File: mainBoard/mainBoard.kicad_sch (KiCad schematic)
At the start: 8 parts, among them Q1 PNP

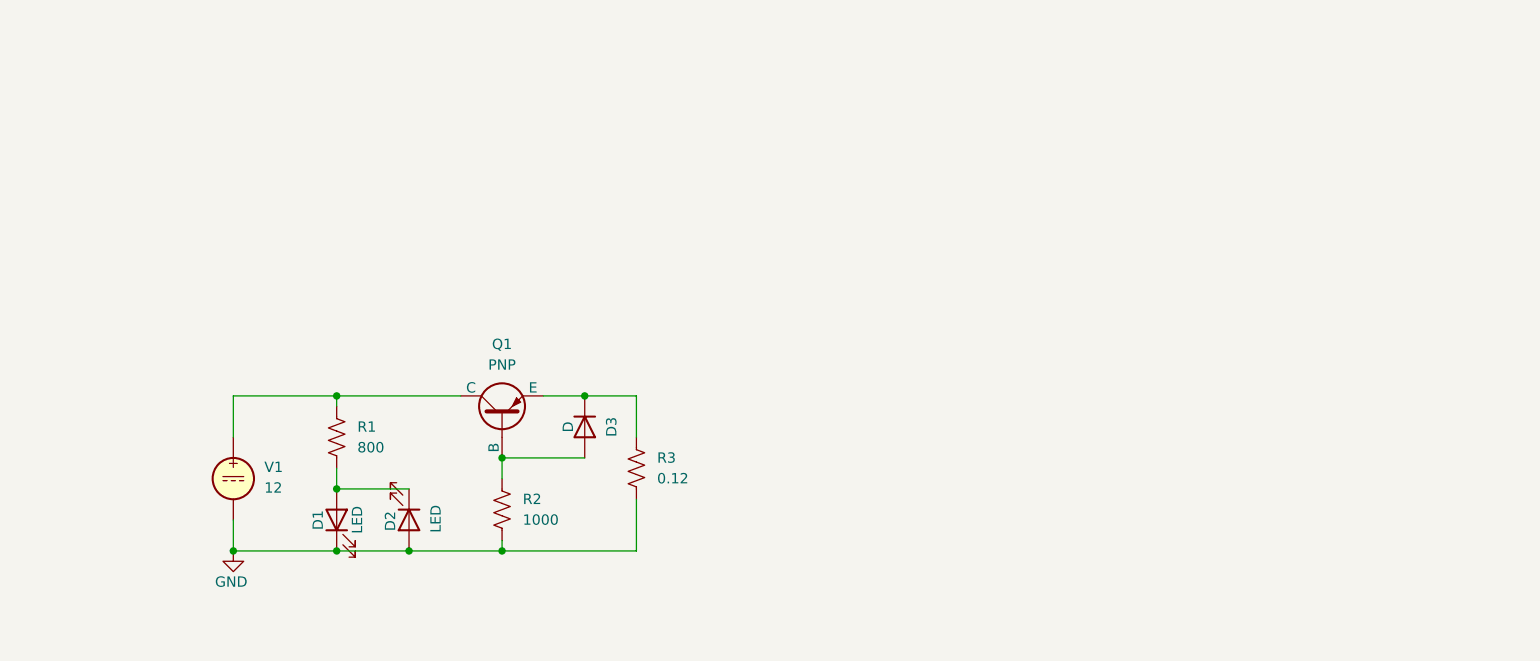
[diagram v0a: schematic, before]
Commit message: Began adding power to the mainboard
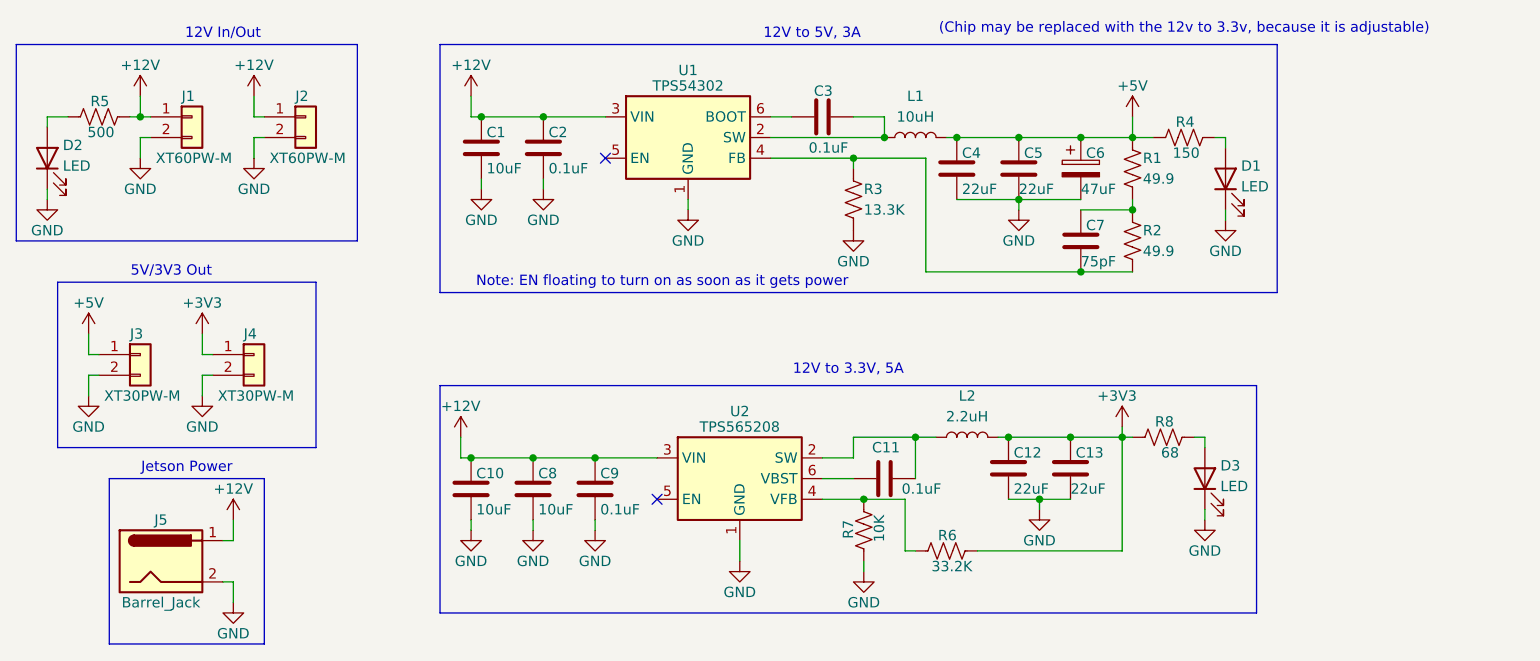
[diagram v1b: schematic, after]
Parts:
- removed D3: D, symbol Simulation_SPICE:D
- removed Q1: PNP, symbol Simulation_SPICE:PNP
- removed V1: 12, symbol Simulation_SPICE:VDC
- added C1, C10, C8: 10uF, Capacitor_SMD:C_0805_2012Metric_Pad1.18x1.45mm_HandSolder, symbol Device:C
- added C11, C2, C3, C9: 0.1uF, Capacitor_SMD:C_0805_2012Metric_Pad1.18x1.45mm_HandSolder, symbol Device:C
- added C12, C13, C4, C5: 22uF, Capacitor_SMD:C_0805_2012Metric_Pad1.18x1.45mm_HandSolder, symbol Device:C
- added C6: 47uF, Capacitor_SMD:CP_Elec_6.3x5.4, symbol Device:C_Polarized
- added C7: 75pF, Capacitor_SMD:C_0805_2012Metric_Pad1.18x1.45mm_HandSolder, symbol Device:C
- added D3: LED, Diode_SMD:D_0805_2012Metric_Pad1.15x1.40mm_HandSolder, symbol Device:LED
- added J1, J2: XT60PW-M, Connector_AMASS:AMASS_XT60PW-M_1x02_P7.20mm_Horizontal, symbol Connector_Generic:Conn_01x02
- added J3, J4: XT30PW-M, Connector_AMASS:AMASS_XT30U-F_1x02_P5.0mm_Vertical, symbol Connector_Generic:Conn_01x02
- added J5: Barrel_Jack, Connector_BarrelJack:BarrelJack_Kycon_KLDX-0202-xC_Horizontal, symbol Connector:Barrel_Jack
- added L1: 10uH, Inductor_SMD:L_Abracon_ASPI-0630LR, symbol Device:L
- added L2: 2.2uH, Inductor_SMD:L_Abracon_ASPI-0630LR, symbol Device:L
- added R4: 150, Resistor_SMD:R_0805_2012Metric_Pad1.20x1.40mm_HandSolder, symbol Device:R_US
- added R5: 500, Resistor_SMD:R_0805_2012Metric_Pad1.20x1.40mm_HandSolder, symbol Device:R_US
- added R6: 33.2K, Resistor_SMD:R_0805_2012Metric_Pad1.20x1.40mm_HandSolder, symbol Device:R_US
- added R7: 10K, Resistor_SMD:R_0805_2012Metric_Pad1.20x1.40mm_HandSolder, symbol Device:R_US
- added R8: 68, Resistor_SMD:R_0805_2012Metric_Pad1.20x1.40mm_HandSolder, symbol Device:R_US
- added U1: TPS54302, Package_TO_SOT_SMD:SOT-23-6, symbol Regulator_Switching:TPS54302
- added U2: TPS565208, Package_TO_SOT_SMD:SOT-23-6, symbol Regulator_Switching:TPS565208
- D1, D2: footprint (none) -> Diode_SMD:D_0805_2012Metric_Pad1.15x1.40mm_HandSolder
- R1: value 800 -> 49.9; footprint (none) -> Resistor_SMD:R_0805_2012Metric_Pad1.20x1.40mm_HandSolder
- R2: value 1000 -> 49.9; footprint (none) -> Resistor_SMD:R_0805_2012Metric_Pad1.20x1.40mm_HandSolder
- R3: value 0.12 -> 13.3K; footprint (none) -> Resistor_SMD:R_0805_2012Metric_Pad1.20x1.40mm_HandSolder
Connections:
- net GND: now also D2.1 (K), R3.2, C1.2, C10.2, C12.2, C13.2, C2.2, C4.2, C5.2, C6.2, C8.2, C9.2, D3.1 (K), J1.2 (Pin_2), J2.2 (Pin_2), J3.2 (Pin_2), J4.2 (Pin_2), J5.2, R7.1, U1.1 (GND), U2.1 (GND); no longer D2.2 (A), R2.1, R3.1
- net at R1.2: now also R2.1, C7.1
- net at R2.2: now also R3.1, C7.2, U1.4 (FB)
- new net: C11.2, L2.1, U2.2 (SW)
- new net: R6.1, R7.2, U2.4 (VFB)
- new net: C11.1, U2.6 (VBST)
- new net: D3.2 (A), R8.2
- new net: D1.2 (A), R4.2
- new net: D2.2 (A), R5.1
- new net: C3.1, U1.6 (BOOT)
- new net: C3.2, L1.1, U1.2 (SW)
- new net +12V: C1.1, C10.1, C2.1, C8.1, C9.1, J1.1 (Pin_1), J2.1 (Pin_1), J5.1, R5.2, U1.3 (VIN), U2.3 (VIN)
- new net +3V3: C12.1, C13.1, J4.1 (Pin_1), L2.2, R6.2, R8.1
- new net +5V: C4.1, C5.1, C6.1, J3.1 (Pin_1), L1.2, R1.1, R4.1
- no-connect marks 0 -> 2
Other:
- note added: "(Chip may be replaced with the 12v to 3.3v, because it is adjustable)"
- note added: "12V In/Out"
- note added: "12V to 3.3V, 5A"
- note added: "12V to 5V, 3A"
- note added: "5V/3V3 Out"
- note added: "Jetson Power"
- note added: "Note: EN floating to turn on as soon as it gets power"

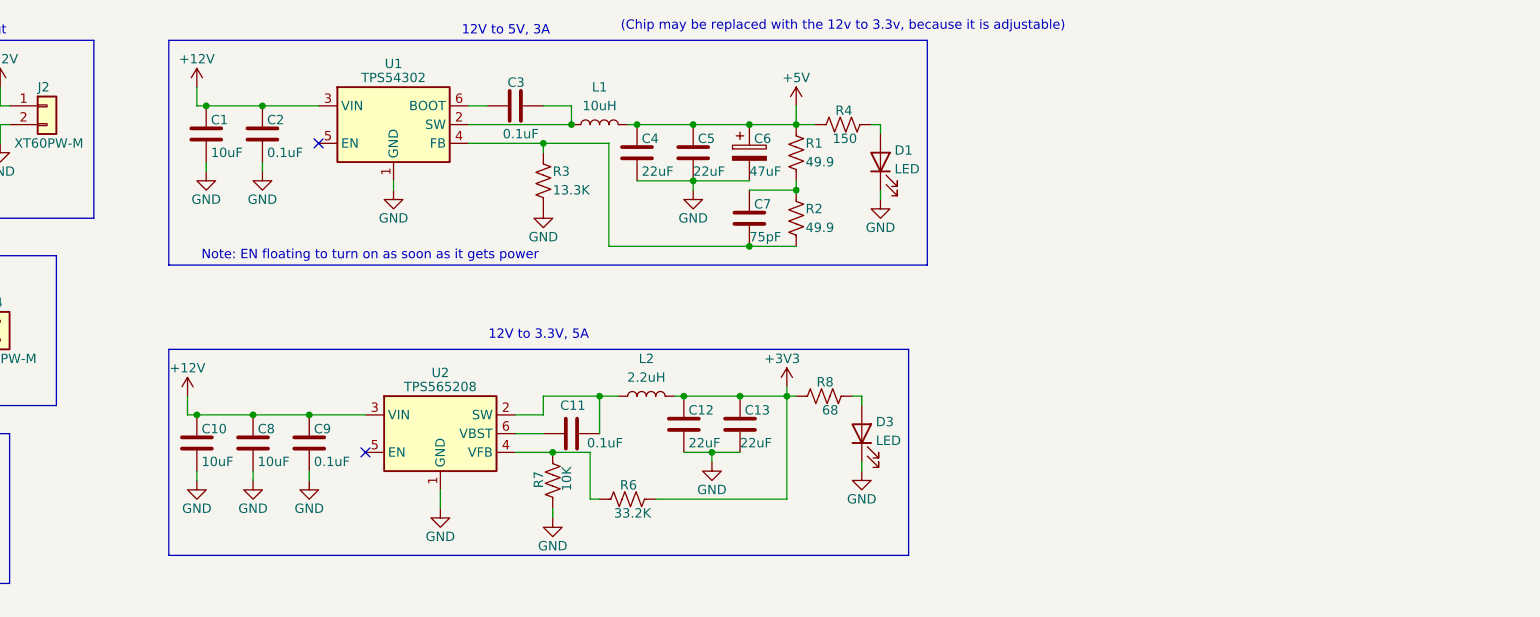
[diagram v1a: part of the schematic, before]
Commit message: Added reverse protection for 5v and 3.3v buck convertors
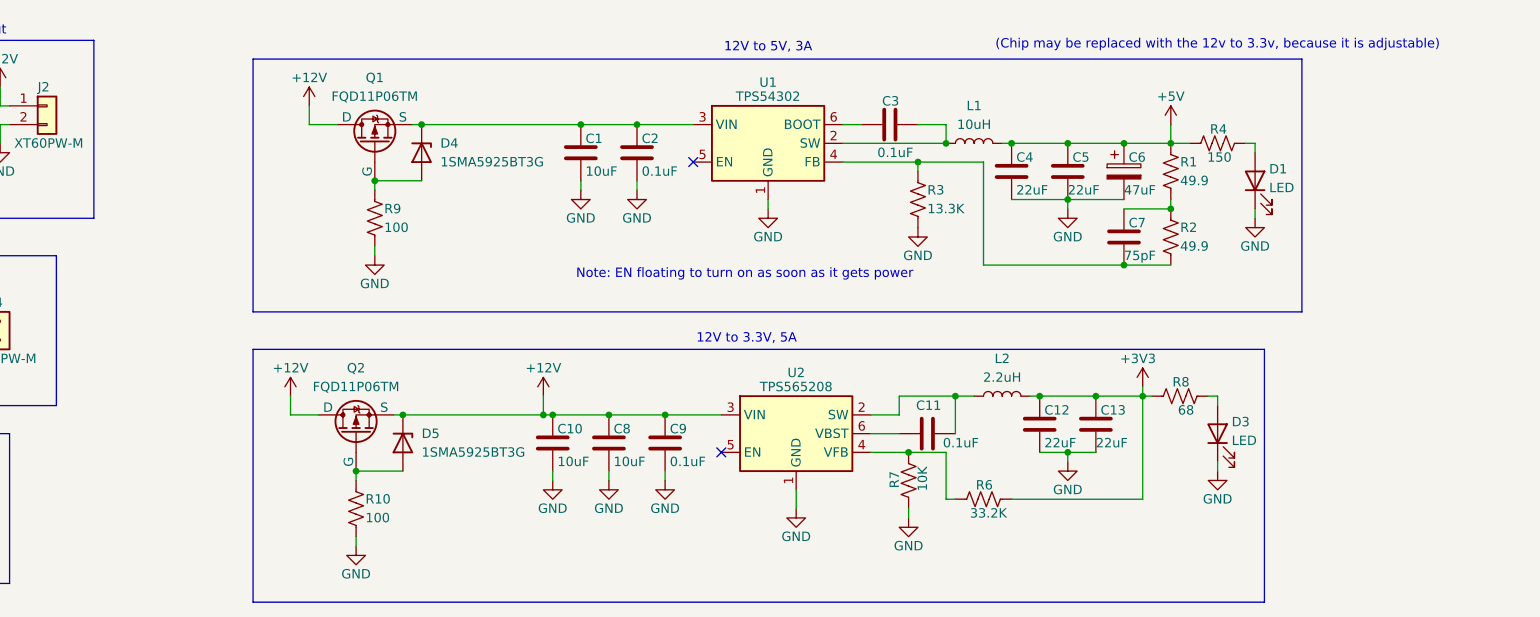
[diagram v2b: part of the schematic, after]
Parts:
- added D4, D5: 1SMA5925BT3G, symbol Device:D_Zener
- added Q1, Q2: FQD11P06TM, Package_TO_SOT_SMD:TO-252-3_TabPin2, symbol Simulation_SPICE:PMOS
- added R10, R9: 100, Resistor_SMD:R_0805_2012Metric_Pad1.20x1.40mm_HandSolder, symbol Device:R_US
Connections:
- net +12V: now also D5.1 (K), Q1.1 (D), Q2.1 (D), Q2.3 (S); no longer C1.1, C2.1, U1.3 (VIN)
- net GND: now also R10.2, R9.2
- new net: D4.2 (A), Q1.2 (G), R9.1
- new net: C1.1, C2.1, D4.1 (K), Q1.3 (S), U1.3 (VIN)
- new net: D5.2 (A), Q2.2 (G), R10.1
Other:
- moved on the sheet: C1, C10, C11, C12, C13, C2, C3, C4, C5, C6, C7, C8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

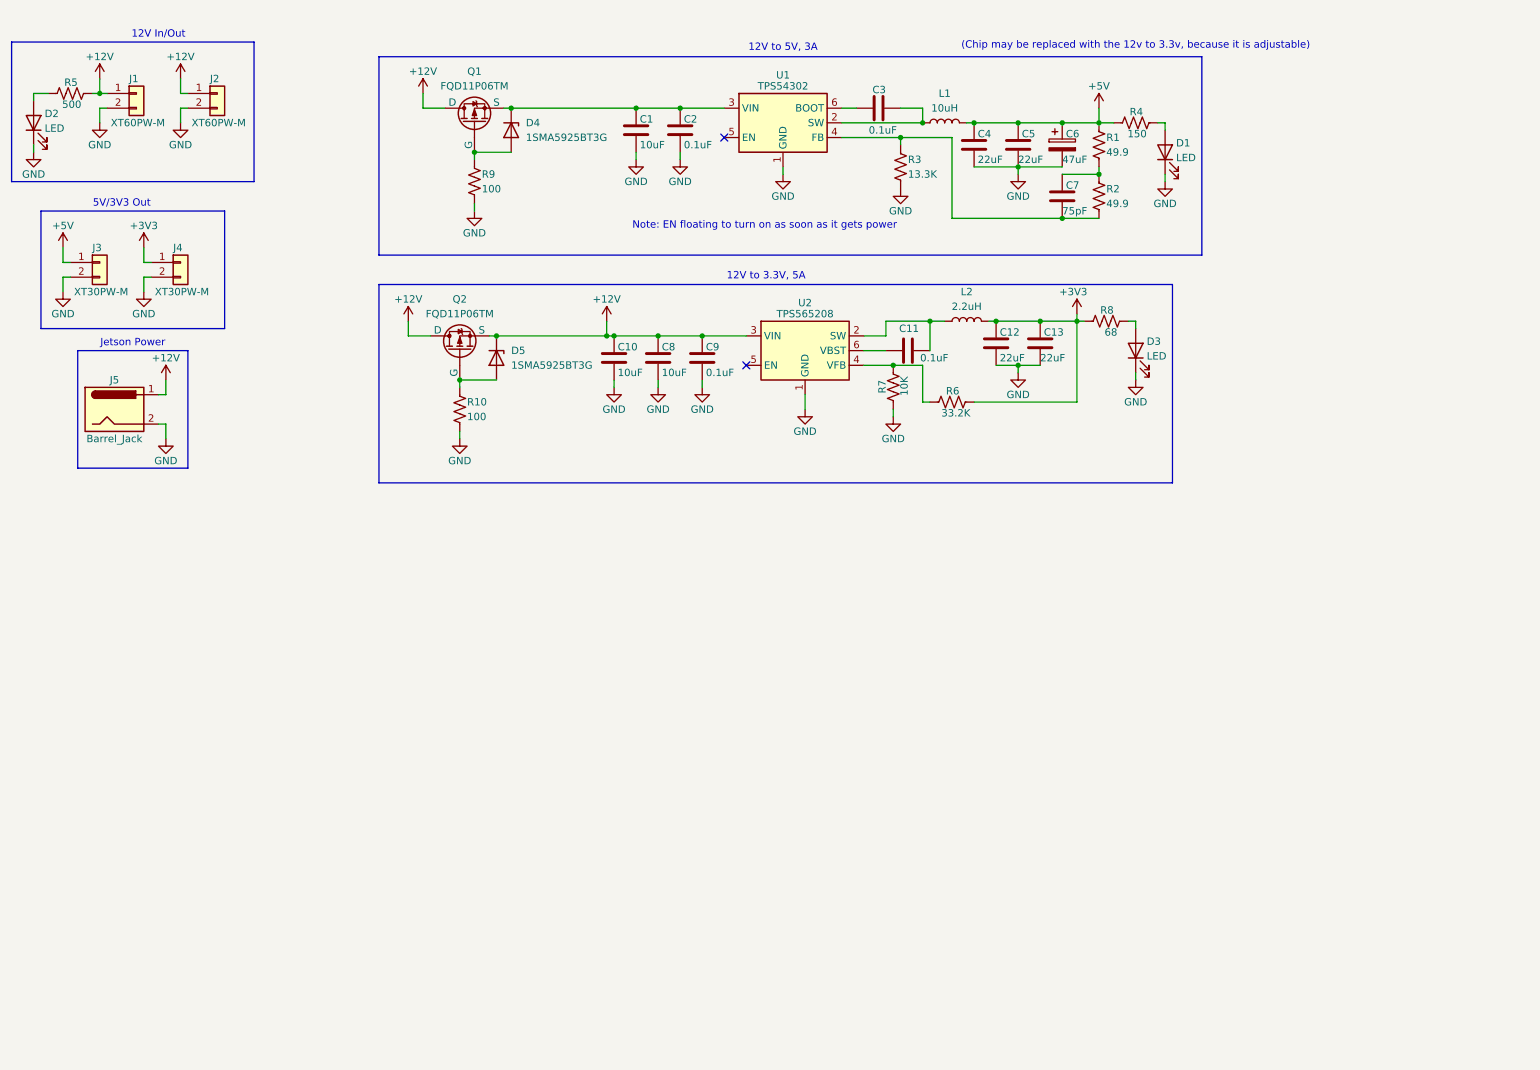
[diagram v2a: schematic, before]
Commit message: Various small things, such as 12v power connectors, jetson header, can stuff, and bypass resistors for reverse protection
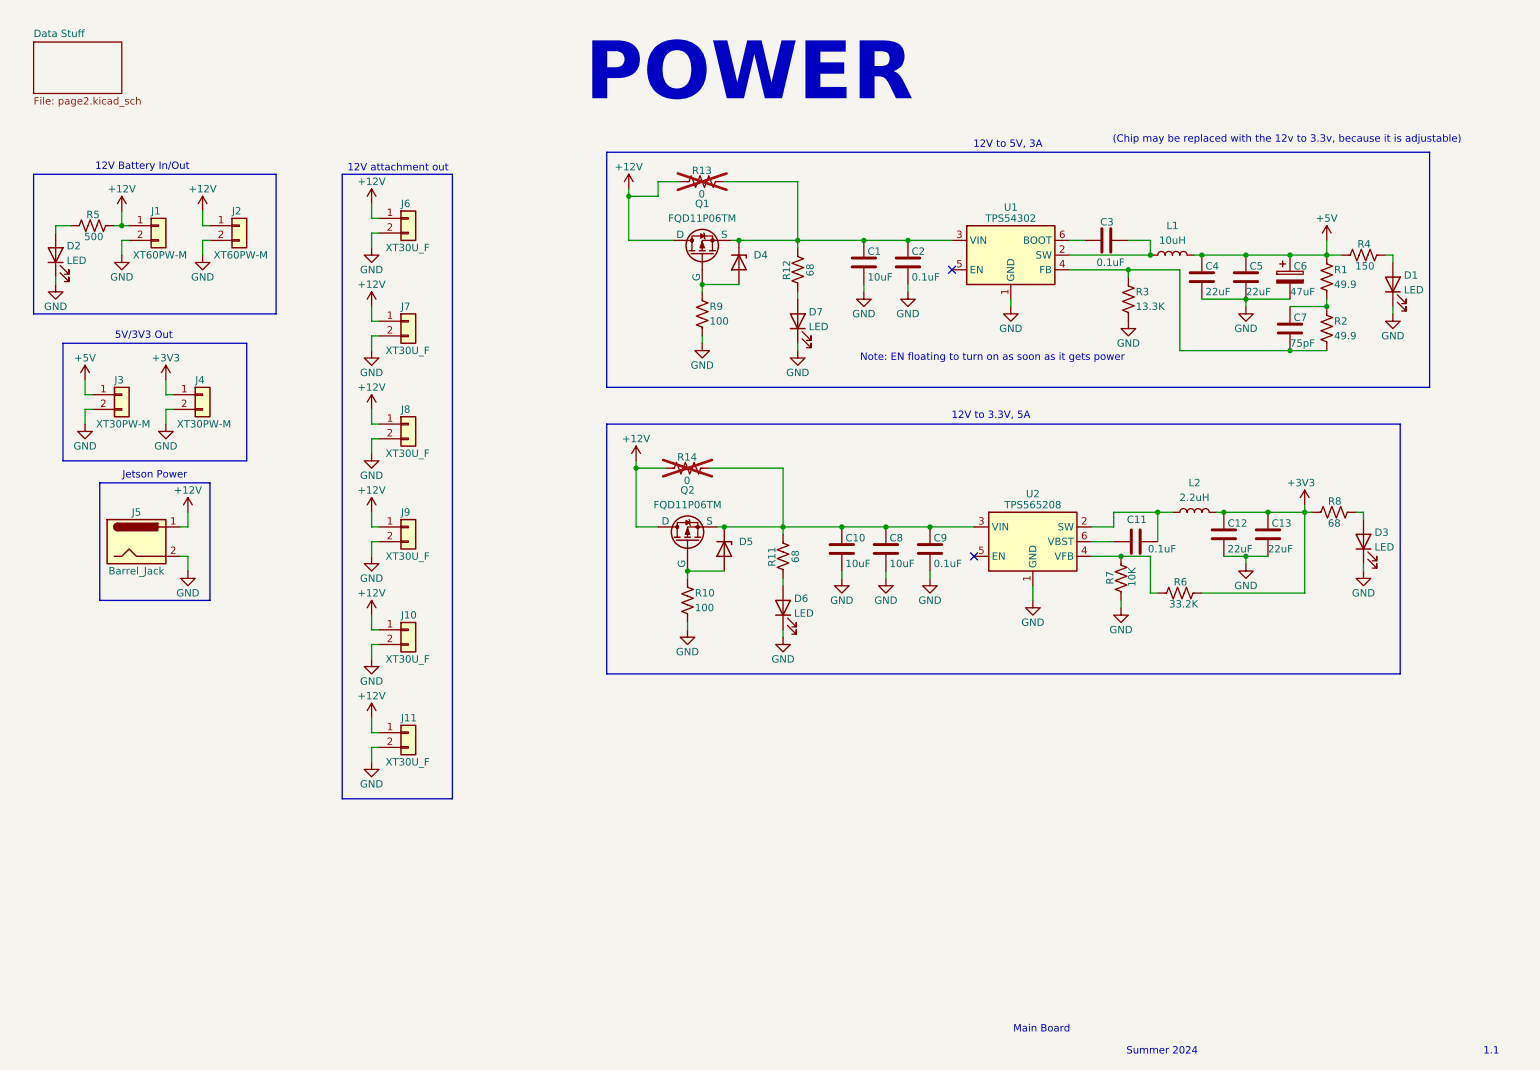
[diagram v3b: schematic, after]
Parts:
- added D6, D7: LED, Diode_SMD:D_0805_2012Metric_Pad1.15x1.40mm_HandSolder, symbol Device:LED
- added J10, J11, J6, J7, J8, J9: XT30U_F, Connector_AMASS:AMASS_XT30U-F_1x02_P5.0mm_Vertical, symbol Connector_Generic:Conn_01x02
- added R11, R12: 68, Resistor_SMD:R_0805_2012Metric_Pad1.20x1.40mm_HandSolder, symbol Device:R_US
- added R13, R14: 0, Resistor_SMD:R_0805_2012Metric_Pad1.20x1.40mm_HandSolder, symbol Device:R_US
- D4, D5: footprint (none) -> Diode_SMD:D_SMA_Handsoldering
- J3, J4: footprint Connector_AMASS:AMASS_XT30U-F_1x02_P5.0mm_Vertical -> Connector_AMASS:AMASS_XT30PW-M_1x02_P2.50mm_Horizontal
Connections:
- net +12V: now also J10.1 (Pin_1), J11.1 (Pin_1), J6.1 (Pin_1), J7.1 (Pin_1), J8.1 (Pin_1), J9.1 (Pin_1), R13.2, R14.2; no longer C10.1, C8.1, C9.1, D5.1 (K), Q2.3 (S), U2.3 (VIN)
- net GND: now also D6.1 (K), D7.1 (K), J10.2 (Pin_2), J11.2 (Pin_2), J6.2 (Pin_2), J7.2 (Pin_2), J8.2 (Pin_2), J9.2 (Pin_2)
- net at C1.1, C2.1, D4.1 (K)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: now also R12.1, R13.1
- new net: C10.1, C8.1, C9.1, D5.1 (K), Q2.3 (S), R11.1, R14.1, U2.3 (VIN)
- new net: D7.2 (A), R12.2
- new net: D6.2 (A), R11.2
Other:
- added sheet Data Stuff (page2.kicad_sch)
- note added: "1.1"
- note added: "12V Battery In/Out"
- note added: "12V attachment out"
- note added: "Main Board"
- note added: "POWER"
- note added: "Summer 2024"
- note removed: "12V In/Out"
- moved on the sheet: C1, C10, C11, C12, C13, C2, C3, C4, C5, C6, C7, C8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
